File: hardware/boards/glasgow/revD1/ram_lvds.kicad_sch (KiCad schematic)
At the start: 36 parts, among them J11 CLK_EXT, J12 FPGA_TP, J6 LVDS, U11 XccelaOPI, U12 XccelaOPI, U8 LFE5U-25F-8BG256x, Y3 Si5351A-B-GM1, Y4 25M

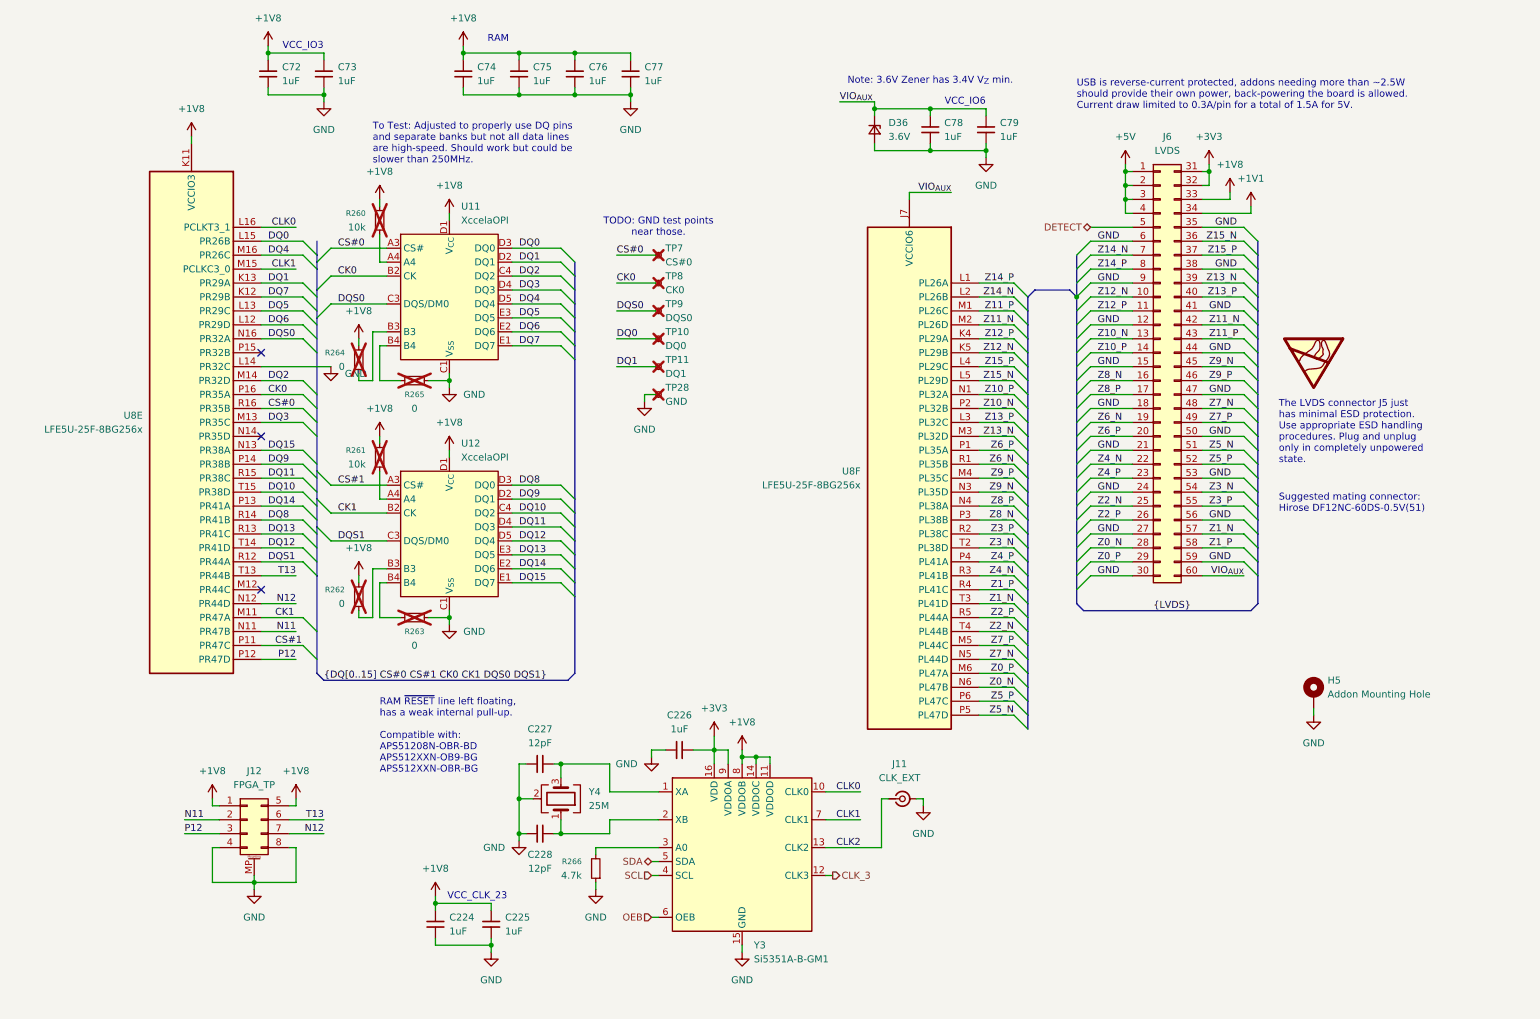
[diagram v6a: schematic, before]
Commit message: misc review changes
disconnect eFuse PG and add comments in schematic as to why
add slew-rate limiting resistor to NAFE clock
add esd diode to external clock output
fix USB D+/D- diff-pairs
update schematic to current date and set revision to D1
fix RAM balls B3/B4 assignment
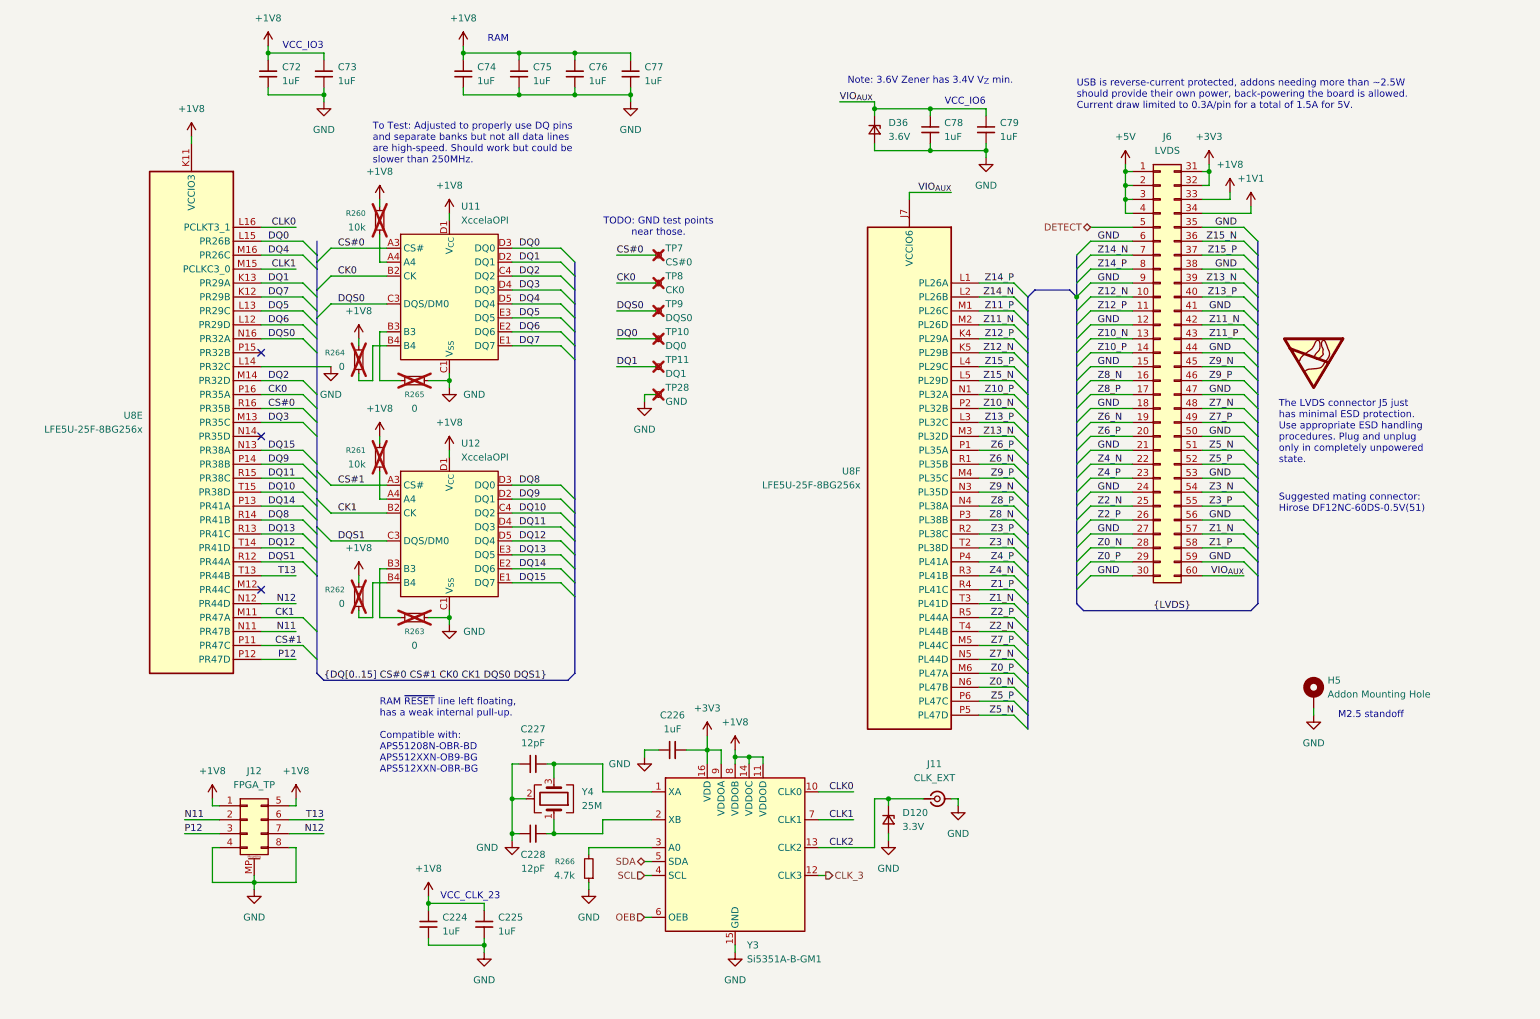
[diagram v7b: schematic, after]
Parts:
- added D120: 3.3V, Diode_SMD:D_0201_0603Metric, symbol Device:D_Zener_Small
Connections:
- net CLK2: now also D120.1 (K)
- net GND: now also D120.2 (A)
- net at R263.1: now also U12.B3; no longer U12.B4
- net at R265.1: now also U11.B3; no longer U11.B4
- net at R262.1: now also U12.B4; no longer U12.B3
- net at R264.1: now also U11.B4; no longer U11.B3
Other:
- note added: "M2.5 standoff"
- moved on the sheet: C224, C225, C226, C227, C228, J11, R266, Y3, Y4
